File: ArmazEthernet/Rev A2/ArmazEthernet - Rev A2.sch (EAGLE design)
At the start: 135 parts, among them J1 22-05-7028-02, P1 RB1-125BAG1A, U1 LM317MDCY, U2 LM317MDCY, U3 KSZ8995MA, U4 AT24C02C-SSHM-B, X1 NE8FAV, X2 NE8FAV, Y1 8Z-25.000MHZMAAJ-T

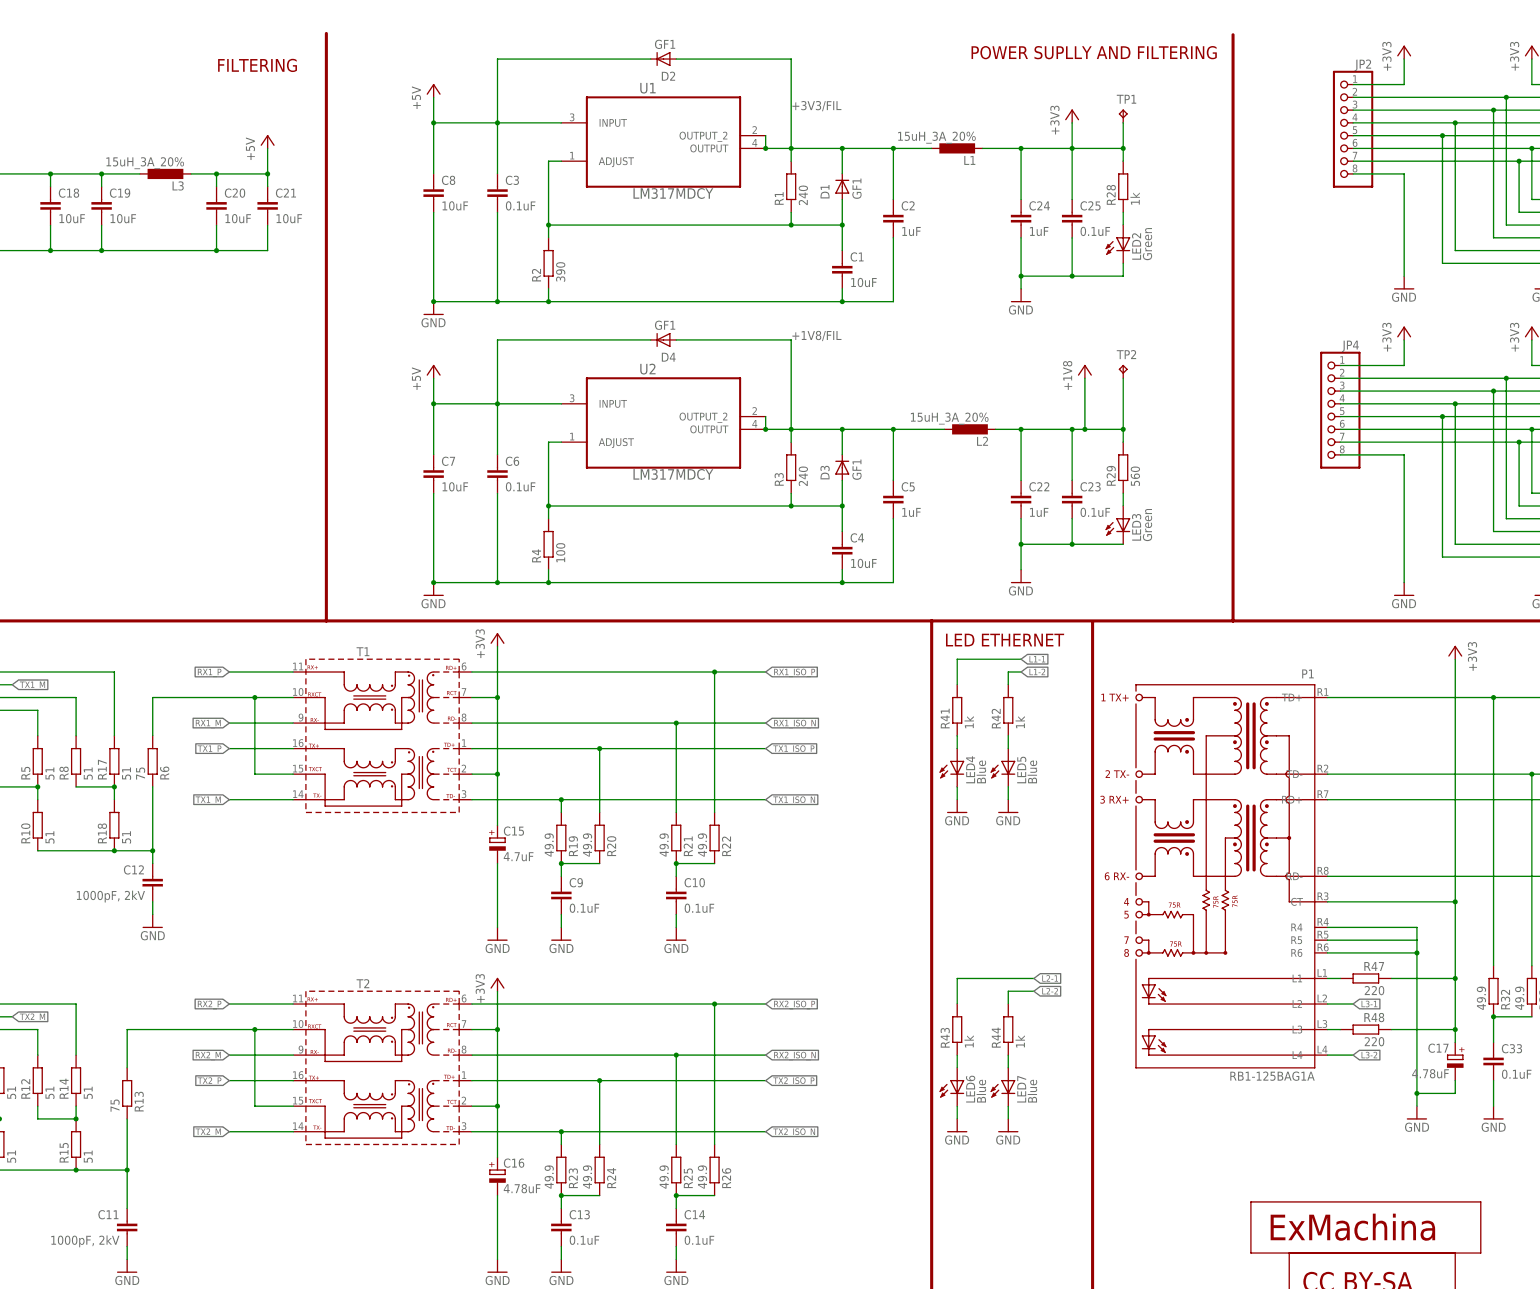
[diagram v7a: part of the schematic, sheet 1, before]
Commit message: Update the route of the board and the schematic
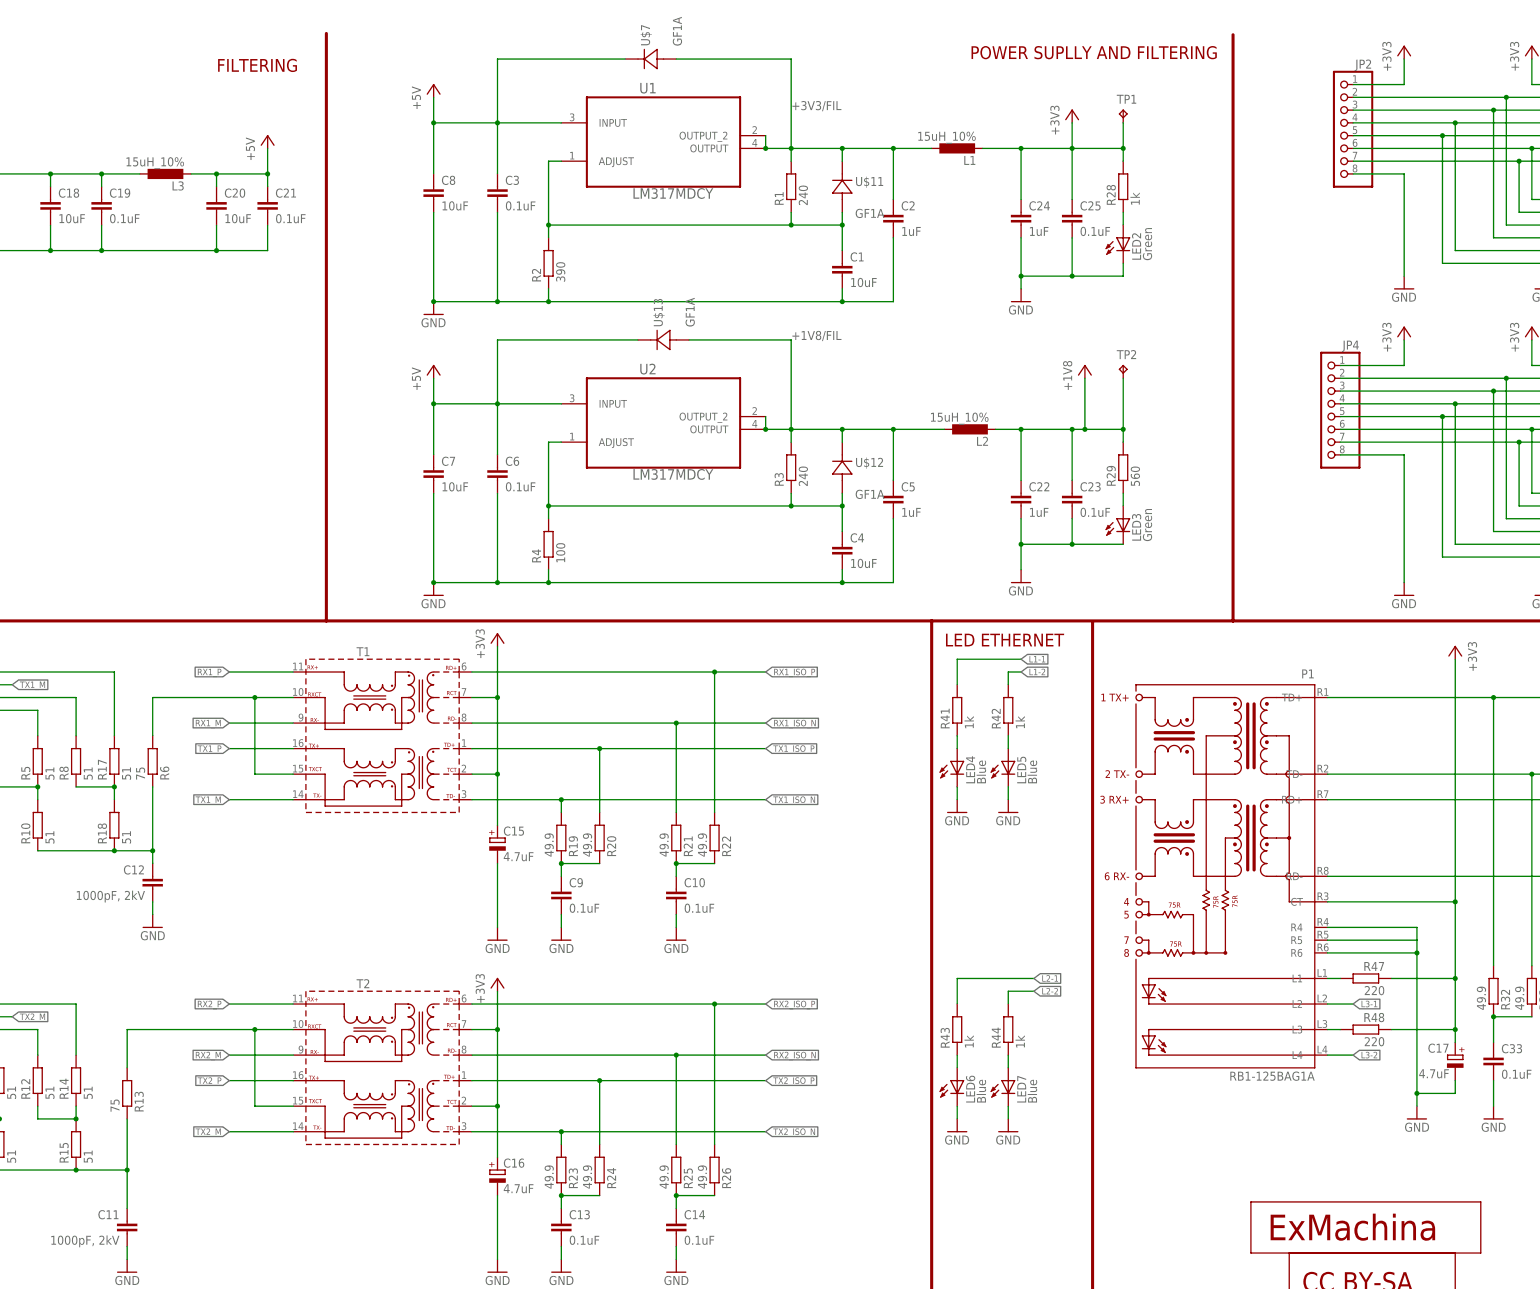
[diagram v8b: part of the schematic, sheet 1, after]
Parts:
- removed D1, D2, D3, D4: GF1, diode:GF1
- added U$11, U$12, U$13, U$7: GF1A, diode:GF1A
- C1, C18, C20, C4, C45, C7, C8: MPN (none) -> MCNP16V106M5X11; OC_NEWARK (none) -> 13M5149
- C10, C11, C12, C13, C14, C15, C2, C22, C23, C24, C25, C26, C27, C28, C29, C3, C30, C31, C32, C33, C34, C35, C36, C37, C38, C39, C40, C41, C42, C43, C44, C46, C47, C5, C6, C9, CR1, JP1, JP2, JP3, JP4, JP5, LED1, LED2, LED3, LED4, LED5, LED6, LED7, P1, R1, R10, R11, R12, R13, R14, R15, R16, R17, R18, R19, R2, R20, R21, R22, R23, R24, R25, R26, R27, R28, R29, R3, R30, R31, R32, R33, R34, R35, R36, R37, R38, R39, R4, R40, R41, R42, R43, R44, R45, R46, R47, R48, R49, R5, R6, R7, R8, R9, T1, T2, TP1, TP2, TP3, TP4, U$5, U$6, U$8, U$9, U3, X1, X2, Y1: OC_NEWARK (none) -> unknown
- C16, C17: value 4.78uF -> 4.7uF; OC_NEWARK (none) -> unknown
- C19, C21: value 10uF -> 0.1uF; OC_NEWARK (none) -> unknown
- L1, L2, L3: value 15uH_3A_20% -> 15uH_10%; OC_NEWARK (none) -> unknown
- U1, U2: MF (none) -> TEXAS INSTRUMENTS
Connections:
- net +1V8/FIL: now also U$12.1, U$13.2; no longer D3.C, D4.A
- net +3V3/FIL: now also U$11.1, U$7.2; no longer D1.C, D2.A
- net +5V: now also U$13.1, U$7.1; no longer D2.C, D4.C
- net N$2: now also U$11.2; no longer D1.A
- net N$6: now also U$12.2; no longer D3.A
